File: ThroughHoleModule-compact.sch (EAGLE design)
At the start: 14 parts, among them IC1 K155ID1, IC2 K155ID1

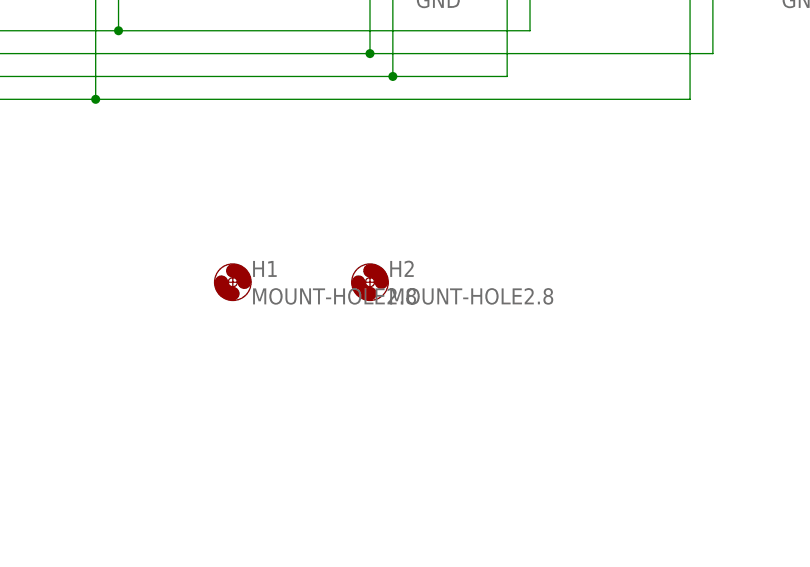
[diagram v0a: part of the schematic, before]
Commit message: Enlarged IN-12 mounting holes
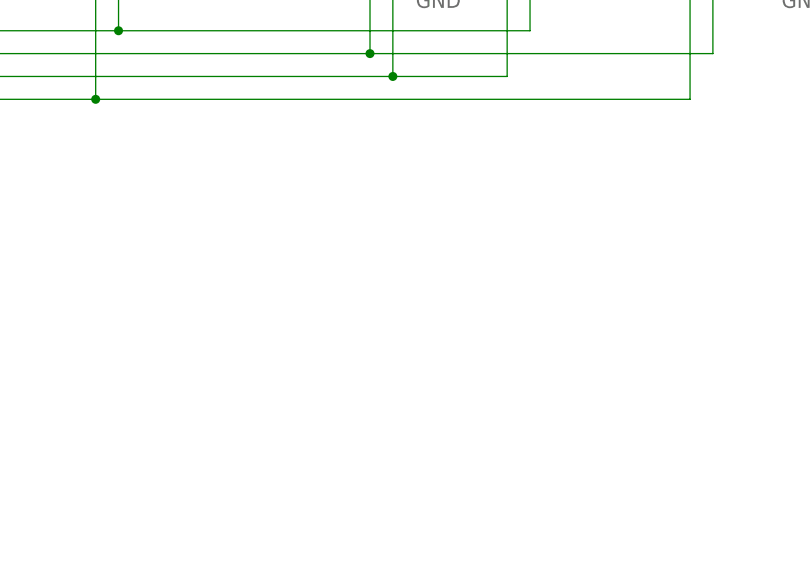
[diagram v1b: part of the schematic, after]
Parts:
- removed H1, H2: MOUNT-HOLE2.8, holes:MOUNT-HOLE2.8
- N1, N2: device mylib:IN-12B -> ThroughHoleModule-compact:IN-12B
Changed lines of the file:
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@@
 <?xml version="1.0" encoding="utf-8"?>
 <!DOCTYPE eagle SYSTEM "eagle.dtd">
-<eagle version="6.1">
+<eagle version="7.7.0">
 <drawing>
 <settings>
@@
 <layer number="54" name="bGND_GNDA" color="1" fill="9" visible="no" active="no"/>
 <layer number="56" name="wert" color="7" fill="1" visible="no" active="no"/>
+<layer number="90" name="Modules" color="5" fill="1" visible="yes" active="yes"/>
 <layer number="91" name="Nets" color="2" fill="1" visible="yes" active="yes"/>
 <layer number="92" name="Busses" color="1" fill="1" visible="yes" active="yes"/>
@@
 </classes>
 <parts>
-<part name="N1" library="mylib" deviceset="IN-12B" device=""/>
-<part name="N2" library="mylib" deviceset="IN-12B" device=""/>
+<part name="N1" library="ThroughHoleModule-compact" deviceset="IN-12B" device=""/>
+<part name="N2" library="ThroughHoleModule-compact" deviceset="IN-12B" device=""/>
 <part name="R1" library="rcl" deviceset="R-EU_" device="0207/10"/>
 <part name="R2" library="rcl" deviceset="R-EU_" device="0207/10"/>
@@
 <part name="JP4" library="pinhead" deviceset="PINHD-2X2" device=""/>
 <part name="JP2" library="pinhead" deviceset="PINHD-2X5" device=""/>
-<part name="H1" library="holes" deviceset="MOUNT-HOLE" device="2.8"/>
-<part name="H2" library="holes" deviceset="MOUNT-HOLE" device="2.8"/>
 <part name="P+2" library="SparkFun" deviceset="VCC" device=""/>
 <part name="GND3" library="SparkFun" deviceset="GND" device=""/>
@@
 <instance part="JP4" gate="A" x="20.32" y="109.22"/>
 <instance part="JP2" gate="A" x="198.12" y="101.6"/>
-<instance part="H1" gate="G$1" x="157.48" y="55.88"/>
-<instance part="H2" gate="G$1" x="172.72" y="55.88"/>
 <instance part="P+2" gate="1" x="177.8" y="111.76"/>
 <instance part="GND3" gate="1" x="220.98" y="88.9"/>
